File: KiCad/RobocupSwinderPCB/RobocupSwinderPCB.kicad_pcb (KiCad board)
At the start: 2 copper layers, 24 parts, among them J1 Barrel_Jack, M1 Stepper_Motor_bipolar, M2 Stepper_Motor_bipolar, SW1 Limit_Switch, SW2 Limit_Switch, SW3 SW_SPST, U1 Teensy4.1, U2 TSR_1-2450

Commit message: A whole lotta stuff.
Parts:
- removed U2: TSR_1-2450, Converter_DCDC:Converter_DCDC_TRACO_TSR-1_THT
- added C5: 0.1uF, Capacitor_SMD:C_1206_3216Metric_Pad1.33x1.80mm_HandSolder, F.Cu at (181.5, 88.4)
- added U3: LM7805_TO220, Package_TO_SOT_SMD:SOT-223, F.Cu at (184.0, 98.8)
- J1: footprint Connector_BarrelJack:BarrelJack_SwitchcraftConxall_RAPC10U_Horizontal -> Library:CONN1x2_PJ-037A_CUD
- moved R1 74.5 mm to (111.0, 122.5), turned to -90 degrees
- moved SW1 67.7 mm to (104.0, 119.0), turned to -90 degrees
- moved R2 67.1 mm to (111.0, 112.5), turned to 90 degrees
- moved U1 59.5 mm to (147.0, 117.0)
- moved SW2 57.7 mm to (104.0, 106.0), turned to -90 degrees
- moved J1 56.0 mm to (186.1, 73.4), turned to 90 degrees
- moved C1 48.3 mm to (114.5, 74.4)
- moved A2 45.6 mm to (168.0, 86.0), turned to -90 degrees
- moved LCD1 41.4 mm to (104.0, 90.0), turned to -90 degrees
- moved RE1 40.3 mm to (103.5, 71.0), turned to -90 degrees
- moved A1 36.7 mm to (141.7, 85.7), turned to -90 degrees
- moved C2 33.6 mm to (146.6, 73.4)
- moved D2 32.4 mm to (199.0, 100.5), turned to -90 degrees
- moved M2 30.4 mm to (166.1, 73.4), turned to 180 degrees
- moved R4 29.4 mm to (198.0, 94.3), turned to -90 degrees
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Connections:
- net Net-(A1-~{FLT}) renamed /Feed_FLT_Pin_22
- net Net-(A1-~{SLP}) renamed /Feed_SLP_Pin_40
- net Net-(A2-STEP) renamed /Coil_STEP_Pin_36
- net Net-(A2-~{FLT}) renamed /Coil_FLT_Pin_21
- net Net-(LCD1-SCL) renamed /LCD_SCL_Pin_19
- net Net-(LCD1-SDA) renamed /LCD_SDA_Pin_18
- net Net-(RE1-CLK) renamed /RE_SW_Pin_21
- net Net-(RE1-DT) renamed /RE_DT_Pin_22
- net Net-(RE1-SW) renamed /RE_CLK_Pin_23
- net Net-(SW2A-B) renamed /LSEnd_Pin_8
- A1 pad 15: Net-(A1-STEP) -> /Feed_STEP_Pin_39
- A1 pad 16: Net-(A1-DIR) -> /Feed_DIR_Pin_38
- A2 pad 14: Net-(A2-~{SLP}) -> /Coil_SLP_Pin_37
- A2 pad 16: Net-(A2-DIR) -> /Coil_DIR_Pin_35
- M1 pad 1: Net-(A1-A1) -> Net-(A1-A2)
- M1 pad 2: Net-(A1-A2) -> Net-(A1-A1)
- M2 pad 1: Net-(A2-A1) -> Net-(A2-A2)
- M2 pad 2: Net-(A2-A2) -> Net-(A2-A1)
- R1 pad 2: Net-(SW1B-C) -> Net-(SW1A-C)
- SW1 pad 1: (no net) -> GND
- SW1 pad 2: (no net) -> /LSStart_Pin_7
- SW1 pad 3: (no net) -> Net-(SW1A-C)
- U1 pad 27: Net-(A2-~{SLP}) -> /Coil_DIR_Pin_35
- U1 pad 29: Net-(A2-DIR) -> /Coil_SLP_Pin_37
- U1 pad 30: Net-(A1-STEP) -> /Feed_DIR_Pin_38
- U1 pad 31: Net-(A1-DIR) -> /Feed_STEP_Pin_39
- U1 pad 7: Net-(SW1B-B) -> /LSStart_Pin_7
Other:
- board outline added: 6 x 2.5 mm

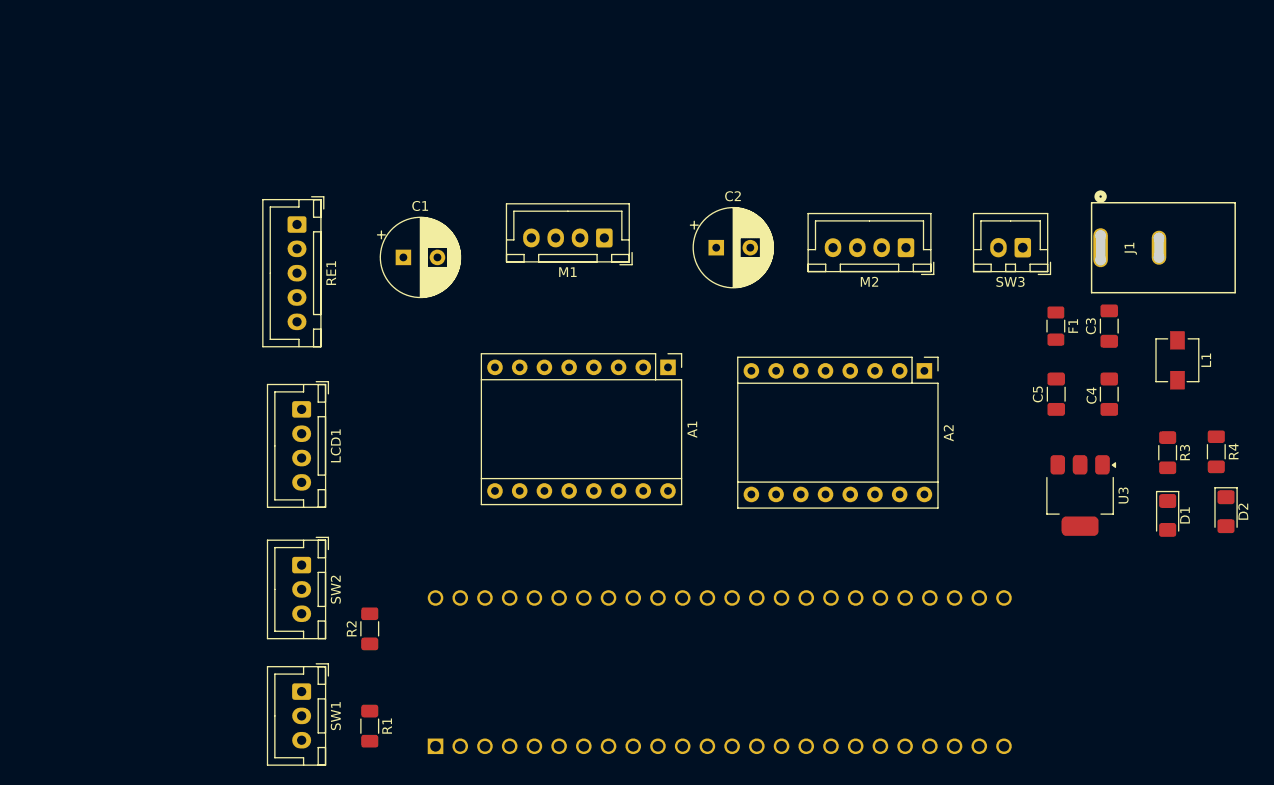
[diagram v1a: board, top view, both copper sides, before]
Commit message: Updated pcb layout.
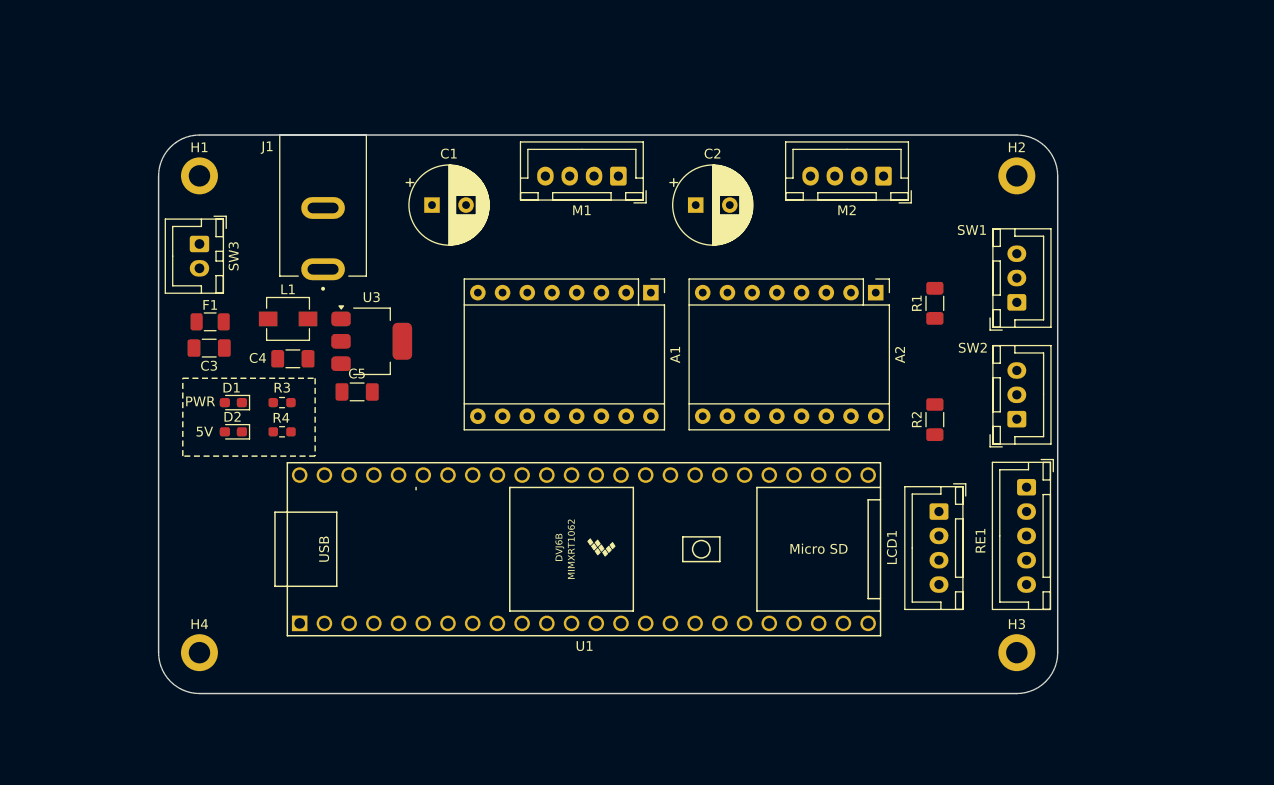
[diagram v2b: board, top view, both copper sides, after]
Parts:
- added H1: MountingHole_Pad, MountingHole:MountingHole_2.2mm_M2_DIN965_Pad, F.Cu at (93.5, 66.0)
- added H2: MountingHole_Pad, MountingHole:MountingHole_2.2mm_M2_DIN965_Pad, F.Cu at (177.5, 66.0)
- added H3: MountingHole_Pad, MountingHole:MountingHole_2.2mm_M2_DIN965_Pad, F.Cu at (177.5, 115.0)
- added H4: MountingHole_Pad, MountingHole:MountingHole_2.2mm_M2_DIN965_Pad, F.Cu at (93.5, 115.0)
- D1, D2: footprint LED_SMD:LED_1206_3216Metric_Pad1.42x1.75mm_HandSolder -> LED_SMD:LED_0603_1608Metric_Pad1.05x0.95mm_HandSolder
- J1: footprint Library:CONN1x2_PJ-037A_CUD -> Library:CUI_PJ-037A
- R3, R4: footprint Resistor_SMD:R_1206_3216Metric_Pad1.30x1.75mm_HandSolder -> Resistor_SMD:R_0603_1608Metric_Pad0.98x0.95mm_HandSolder
- U1: footprint TeensyLibrary:Teensy4.1 Pins-only -> TeensyLibrary:Teensy41-Pins-Only_Silkscreen
- moved D2 102.3 mm to (97.0, 92.3), turned to 180 degrees
- moved D1 96.7 mm to (97.0, 89.3), turned to 180 degrees
- moved R4 96.0 mm to (102.0, 92.3), turned to 0 degrees
- moved C3 92.5 mm to (94.5, 83.7), turned to 180 degrees
- moved L1 91.5 mm to (102.6, 80.7), turned to 0 degrees
- moved R3 91.2 mm to (102.0, 89.3), turned to 180 degrees
- moved F1 86.9 mm to (94.6, 81.0), turned to 0 degrees
- moved SW3 84.6 mm to (93.5, 73.0), turned to -90 degrees
- moved C4 84.0 mm to (103.1, 84.8), turned to 180 degrees
- moved SW1 83.7 mm to (177.5, 79.0), turned to 90 degrees
- moved J1 79.9 mm to (106.2, 75.6)
- moved RE1 79.7 mm to (178.5, 98.0)
- moved SW2 75.0 mm to (177.5, 91.0), turned to 90 degrees
- moved U3 74.5 mm to (111.2, 83.0), turned to 0 degrees
- moved R1 72.5 mm to (169.1, 79.1), turned to 90 degrees
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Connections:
- LCD1 pad 3: /LCD_SCL_Pin_19 -> /LCD_SDA_Pin_18
- LCD1 pad 4: /LCD_SDA_Pin_18 -> /LCD_SCL_Pin_19
- R1 pad 2: Net-(SW1A-C) -> /NO_LS1
- R2 pad 2: Net-(SW2A-C) -> /NO_LS2
- SW1 pad 1: GND -> /LSStart_Pin_7
- SW1 pad 2: /LSStart_Pin_7 -> /NO_LS1
- SW1 pad 3: Net-(SW1A-C) -> GND
- SW2 pad 1: GND -> /LSEnd_Pin_8
- SW2 pad 2: /LSEnd_Pin_8 -> /NO_LS2
- SW2 pad 3: Net-(SW2A-C) -> GND
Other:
- board size 6 x 2.5 mm -> 92.4 x 57.4 mm
- board text added: "5V"
- board text added: "PWR"

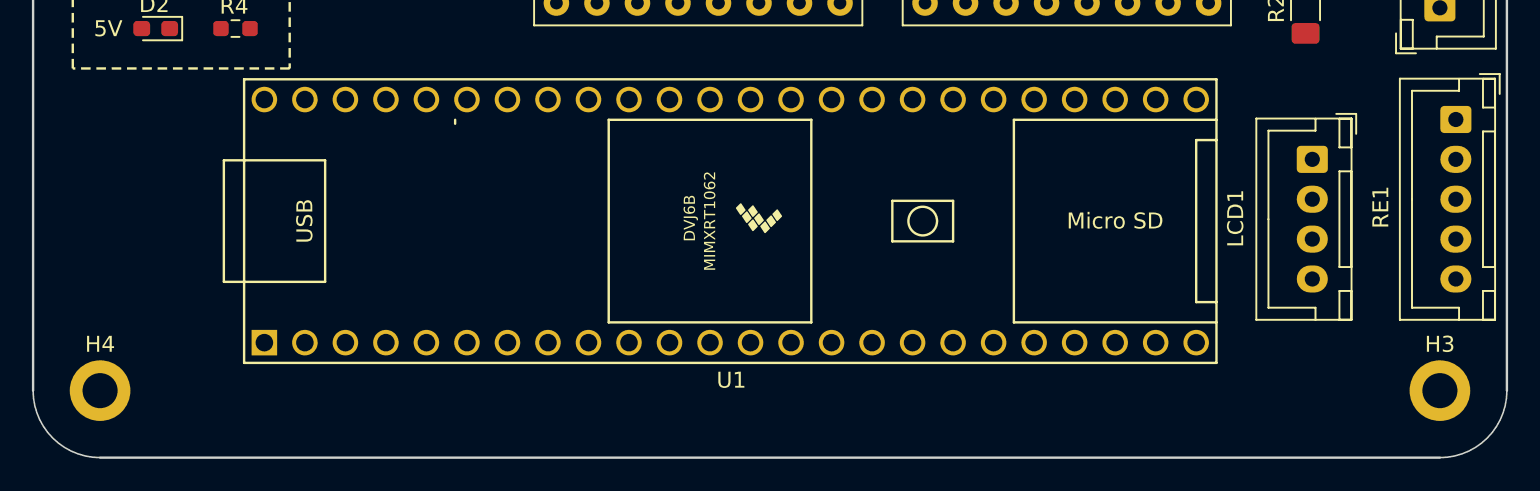
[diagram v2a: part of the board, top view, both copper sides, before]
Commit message: Added buzz silkscreen.
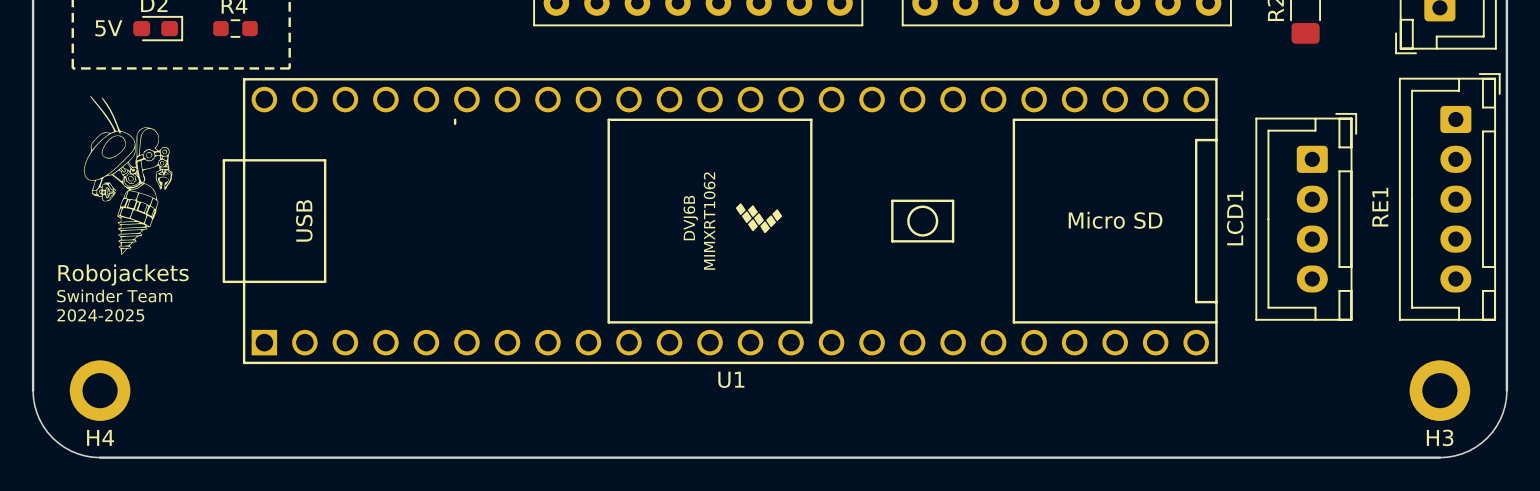
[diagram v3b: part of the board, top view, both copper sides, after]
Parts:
- added G***: LOGO, Library:RoboBuzz, F.Cu at (95.2, 101.5)
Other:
- board text added: "Robojackets"
- board text added: "Swinder Team 2024-2025"

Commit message: Routing.
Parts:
- moved J1 0.40 mm to (106.2, 76.0)
- moved SW3 0.20 mm to (93.7, 73.0)
- moved M1 0.20 mm to (136.6, 66.2)
- moved M2 0.20 mm to (163.8, 66.2)
- moved RE1 0.20 mm to (178.3, 98.0)
- moved SW1 0.20 mm to (177.3, 79.0)
- moved SW2 0.20 mm to (177.3, 91.0)
- turned R3 to 0 degrees
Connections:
- A1 pad 2: /Feed_FLT_Pin_22 -> /Feed_FLT_Pin_21
- A2 pad 2: /Coil_FLT_Pin_21 -> /Coil_FLT_Pin_22
- U1 pad 21: /Coil_FLT_Pin_21 -> /Feed_FLT_Pin_21
- U1 pad 22: /Feed_FLT_Pin_22 -> /Coil_FLT_Pin_22
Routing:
- net +5V: track 0.00 -> 156.7 mm, vias 0 -> 2
- net +3.3V: track 0.00 -> 88.9 mm, vias 0 -> 2
- net /LSStart_Pin_7: track 0.00 -> 79.8 mm, vias 0 -> 1
- net /RE_CLK_Pin_23: track 0.00 -> 75.2 mm
- net /RE_DT_Pin_22: track 0.00 -> 72.9 mm
- net /RE_SW_Pin_21: track 0.00 -> 70.5 mm
- net /LSEnd_Pin_8: track 0.00 -> 68.8 mm, vias 0 -> 1
- net VCC: track 0.00 -> 67.2 mm, vias 0 -> 1
- net /Feed_FLT_Pin_21: track 0.00 -> 63.2 mm, vias 0 -> 4
- net /LCD_SCL_Pin_19: track 0.00 -> 52.6 mm
- net /LCD_SDA_Pin_18: track 0.00 -> 49.0 mm
- net /Coil_FLT_Pin_22: track 0.00 -> 41.1 mm, vias 0 -> 4
- net GND: track 0.00 -> 19.2 mm, vias 0 -> 5
- net Net-(A2-A2): track 0.00 -> 15.1 mm
- net Net-(A2-B2): track 0.00 -> 14.5 mm
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- added copper zone on B.Cu, net GND
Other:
- board size 92.4 x 57.4 mm -> 92 x 57 mm
- board text added: "49mm"
- board text added: "57mm"
- board text added: "84mm"
- board text added: "92mm"
- board text added: "Designed By: Jaxon Parriott and Swathi Padmanabhan"
- board text added: "Rev: 1"
